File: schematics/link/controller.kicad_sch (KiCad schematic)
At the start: 55 parts, among them J6 Prog_Header, J7 SPI1, J8 SPI2, J9 Clock Jumper, SW5 BOOT0, SW6 RESET, U10 AT25SF128A-SHB-T, U7 ADS131M02QPWRQ1, U8 STM32G031K8Tx, U9 W5500, Y1 ECS-2520MVLC-081.92-BN-TR, Y2 KC2520Z25.0000C1SY00;

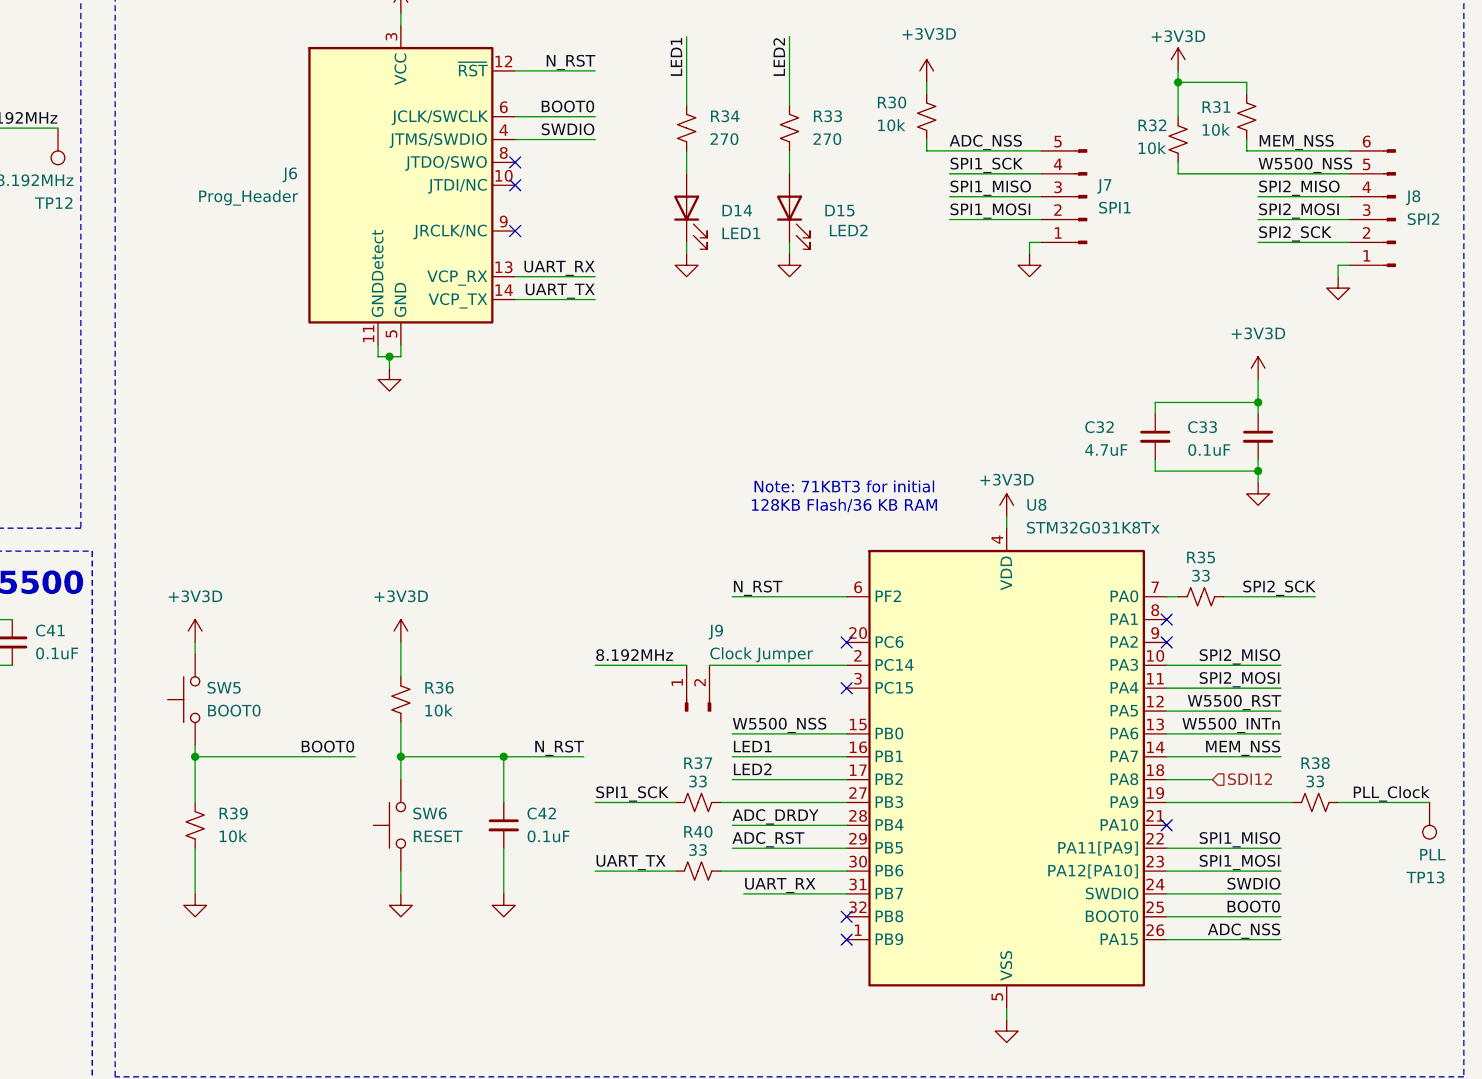
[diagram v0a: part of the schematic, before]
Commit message: update(pcb): combining modules
Want to try a different layout, but like where I am at right now
Planning to branch off of this one and see where it goes
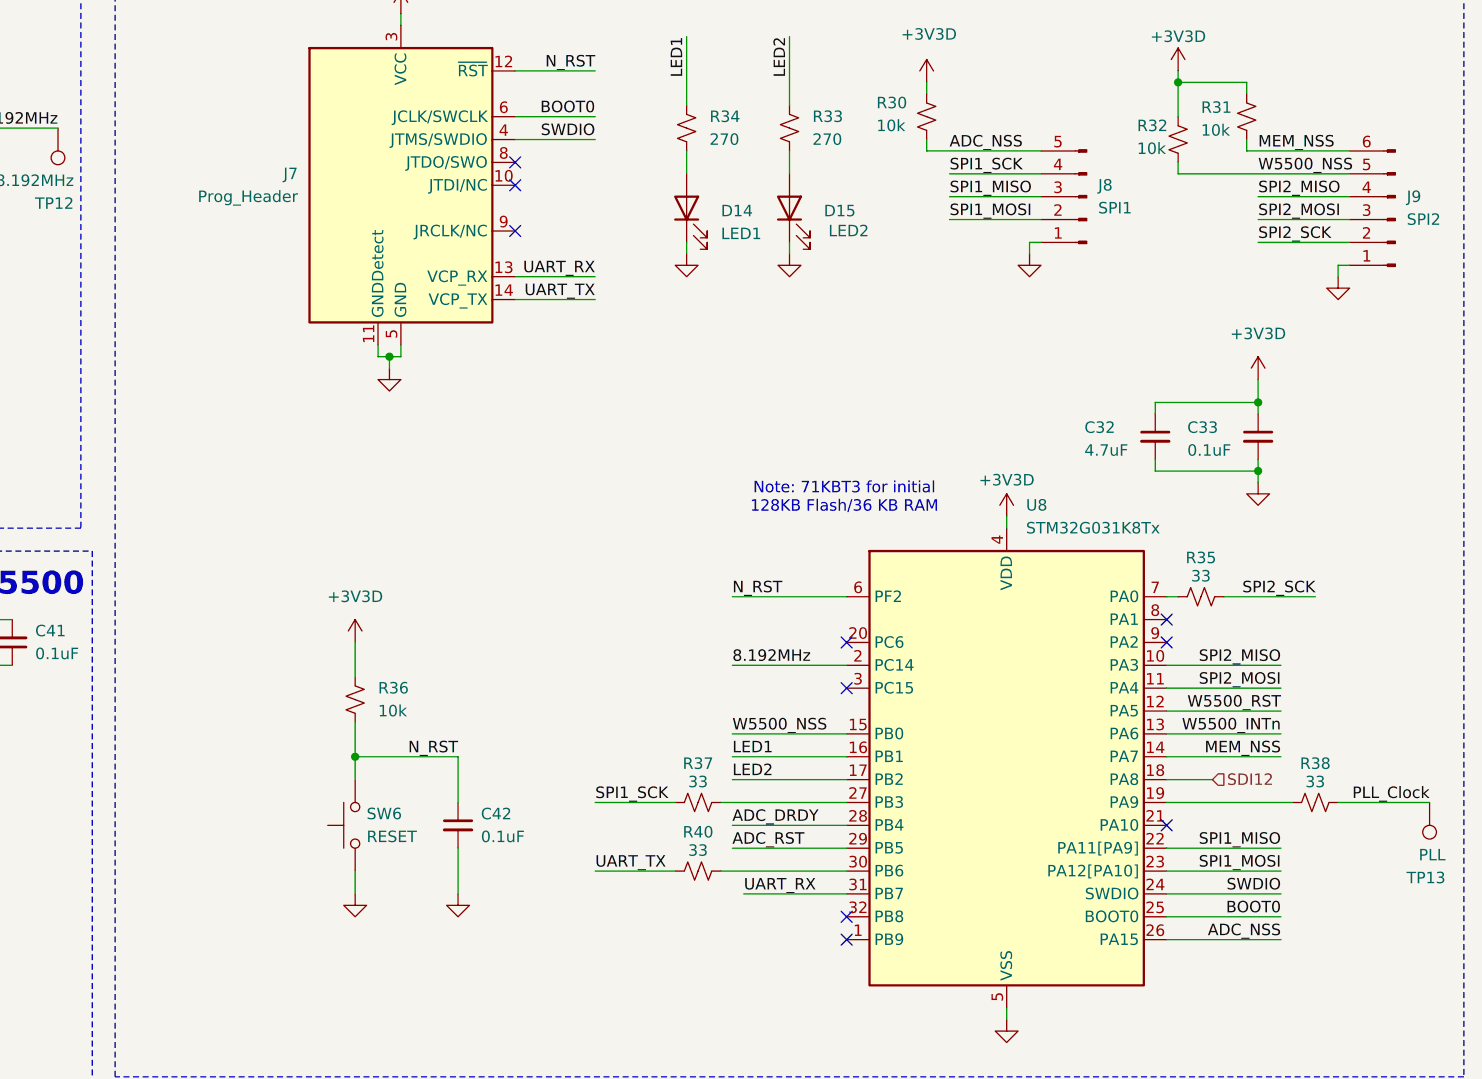
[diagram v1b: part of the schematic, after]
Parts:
- removed J9: Clock Jumper, Connector_PinHeader_2.54mm:PinHeader_1x02_P2.54mm_Vertical, symbol Connector:Conn_01x02_Pin
- removed R39: 10k, Resistor_SMD:R_0603_1608Metric, symbol Device:R_Small_US
- removed SW5: BOOT0, Link_Footprints:SW_TS04-66-55-BK-260-SMT, symbol Switch:SW_Push
- C32: footprint Capacitor_SMD:C_0402_1005Metric -> Capacitor_SMD:C_0603_1608Metric
- R30, R31, R32, R36, R41, R42: footprint Resistor_SMD:R_0603_1608Metric -> Resistor_SMD:R_0402_1005Metric
- renumbered J6 to J7, J7 to J8, J8 to J9
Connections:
- net 8.192MHz: now also U8.2 (PC14)
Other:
- moved on the sheet: C42, R36, SW6

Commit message: update(link): finalized placements
Still some work to be done:
1. Fix planes under RJ45 connector, probably should keep out if possible
2. Fix silkscreening
3. Fix isolated filled zones
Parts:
- removed C26, C28: 0.1uF, Capacitor_SMD:C_0402_1005Metric, symbol Device:C_Small
- removed D15: LED2, Diode_SMD:D_0603_1608Metric, symbol Device:LED
- removed J8: SPI1, Connector_PinHeader_2.54mm:PinHeader_1x05_P2.54mm_Vertical, symbol Connector:Conn_01x05_Pin
- removed J9: SPI2, Connector_PinHeader_2.54mm:PinHeader_1x06_P2.54mm_Vertical, symbol Connector:Conn_01x06_Pin
- removed R32: 10k, Resistor_SMD:R_0402_1005Metric, symbol Device:R_Small_US
- removed R34: 270, Resistor_SMD:R_0603_1608Metric, symbol Device:R_Small_US
- removed R40: 33, Resistor_SMD:R_0402_1005Metric, symbol Device:R_Small_US
- added R36: 10k, Resistor_SMD:R_0402_1005Metric, symbol Device:R_Small_US
- added R38: 33, Resistor_SMD:R_0402_1005Metric, symbol Device:R_Small_US
- R30: value 10k -> 270; footprint Resistor_SMD:R_0402_1005Metric -> Resistor_SMD:R_0603_1608Metric; LCSC Part # C95204 -> (none)
- R33: value 270 -> 10k; footprint Resistor_SMD:R_0603_1608Metric -> Resistor_SMD:R_0402_1005Metric; LCSC Part # C22369858 -> C95204; MPN RCA03270RFLF -> (none)
- R37: value 33 -> 10k; LCSC Part # C25105 -> C95204
- renumbered C29 to C27, C25 to C28, C30 to C29, C27 to C30, D14 to D10, J7 to J6, R36 to R32, R38 to R34, R41 to R39, R42 to R40, R43 to R41, SW6 to SW5
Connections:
- net +3V3A: now also U7.1 (AVDD)
- net +3V3A1: no longer U7.1 (AVDD)
- net +3V3D: now also R33.1, R37.1, R36.1; no longer R30.1
- net ADC_DRDY: now also U8.20 (PC6); no longer U8.28 (PB4)
- net ADC_NSS: now also R37.2; no longer R30.2
- net ADC_RST: now also U8.21 (PA10); no longer U8.29 (PB5)
- net MEM_NSS: now also U8.7 (PA0); no longer U8.14 (PA7)
- net SDI12: now also U8.9 (PA2); no longer U8.18 (PA8)
- net SPI1_SCK: now also R35.2; no longer R37.1
- net SPI2_MISO: now also U8.30 (PB6); no longer U8.10 (PA3)
- net SPI2_MOSI: now also U8.31 (PB7); no longer U8.11 (PA4)
- net SPI2_SCK: now also R38.2; no longer R35.2
- net UART_RX: now also U8.15 (PB0); no longer U8.31 (PB7)
- net UART_TX: now also U8.12 (PA5)
- net W5500_INTn: now also U8.28 (PB4); no longer U8.13 (PA6)
- net W5500_NSS: now also R33.2, U8.29 (PB5); no longer U8.15 (PB0)
- net W5500_RST: now also U8.1 (PB9), R36.2; no longer U8.12 (PA5)
- net at U8.27 (PB3): now also R35.1; no longer R37.2
- net at D10.2 (A): now also R30.2
- net at R34.1: now also U8.18 (PA8); no longer U8.19 (PA9)
- net at U8.32 (PB8): now also R38.1
- net LED1: no longer names the net of U8.16 (PB1)
- net LED2: no longer names the net of U8.17 (PB2)
- net LED2: no longer R33.1
- new net STATUS: R30.1, U8.10 (PA3)
- no-connect marks 22 -> 23
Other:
- moved on the sheet: C28, C30, C42, R32, R34, SW5, TP13

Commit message: fix: git history
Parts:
- added TP16, TP17: GND, Link_Footprints:TestPoint_Pad_D1.5mm, symbol Connector:TestPoint
- C42: MPN CGA0603X7R104K500JT -> (none)
- D10: MPN KT-0603B -> (none)
- R32: MPN RCA0310KJLF -> (none)
- SW5: MPN TS04-66-55-BK-260-SMT -> (none)
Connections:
- net GND: now also TP16.1, TP17.1
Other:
- note removed: "Note: 71KBT3 for initial 128KB Flash/36 KB RAM"

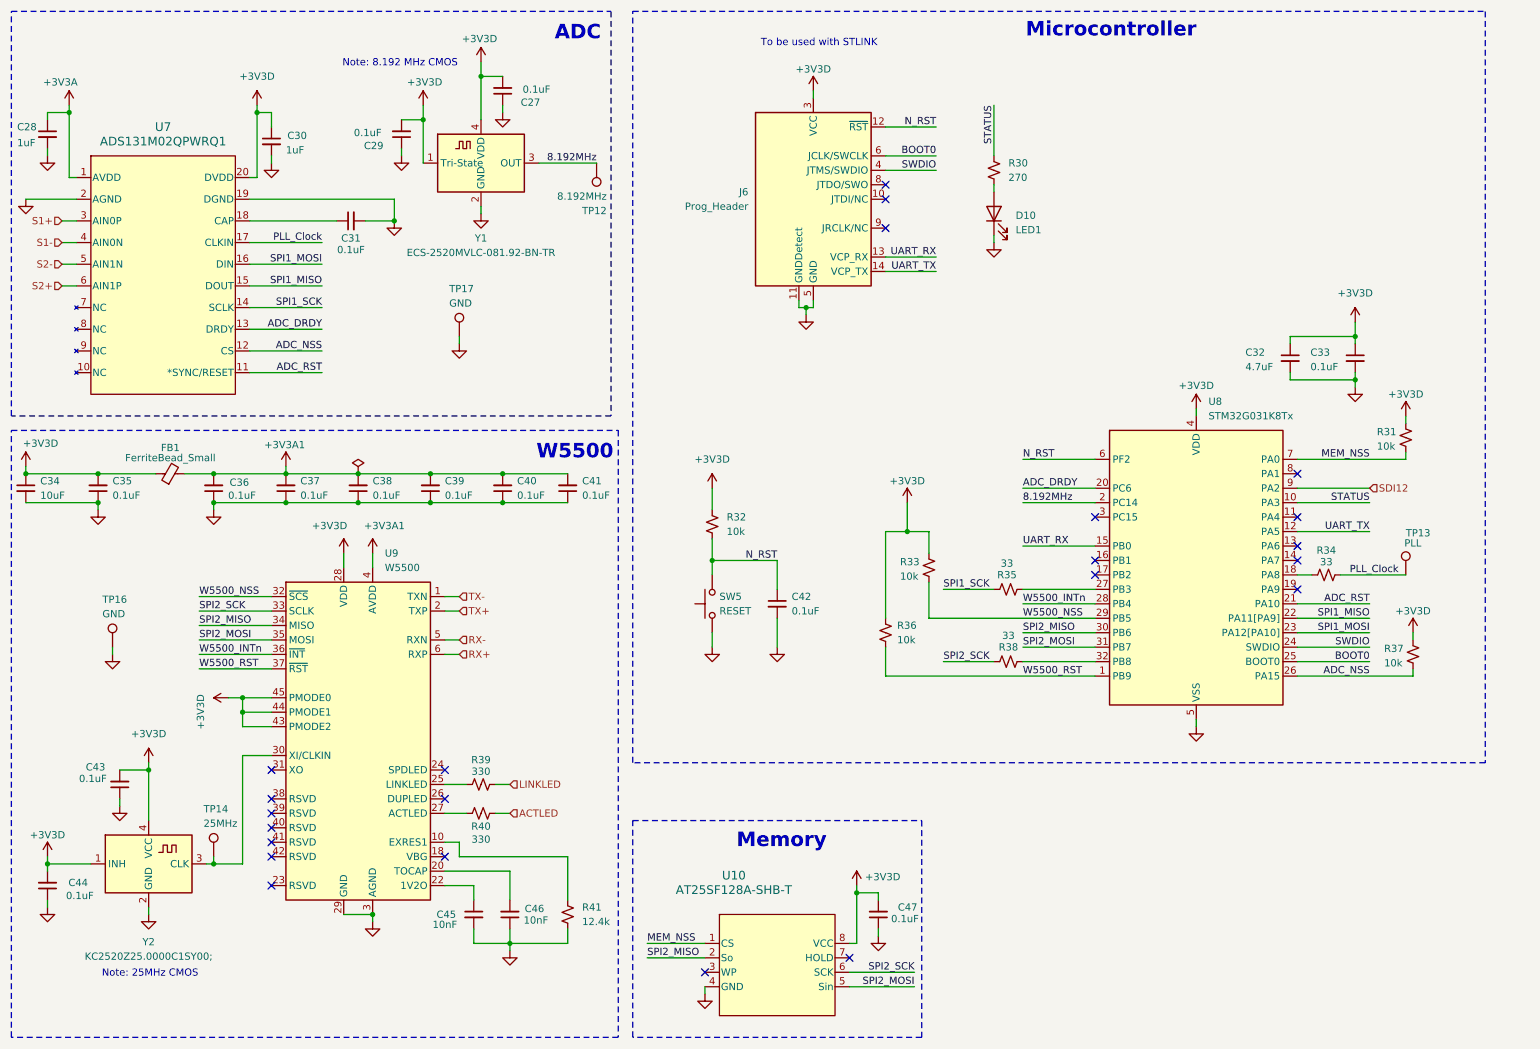
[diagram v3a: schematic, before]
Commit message: update(review):
1. Take gain resistor out of AFE filter
2. Breakout I2C
3. Move fuse to cover both 12V rails
4. Silkscreens
5. More testpoints + change to clip ons
6. Match ADC input max and filter output max
7. Add shunt for current resistors
8. Thermocouples
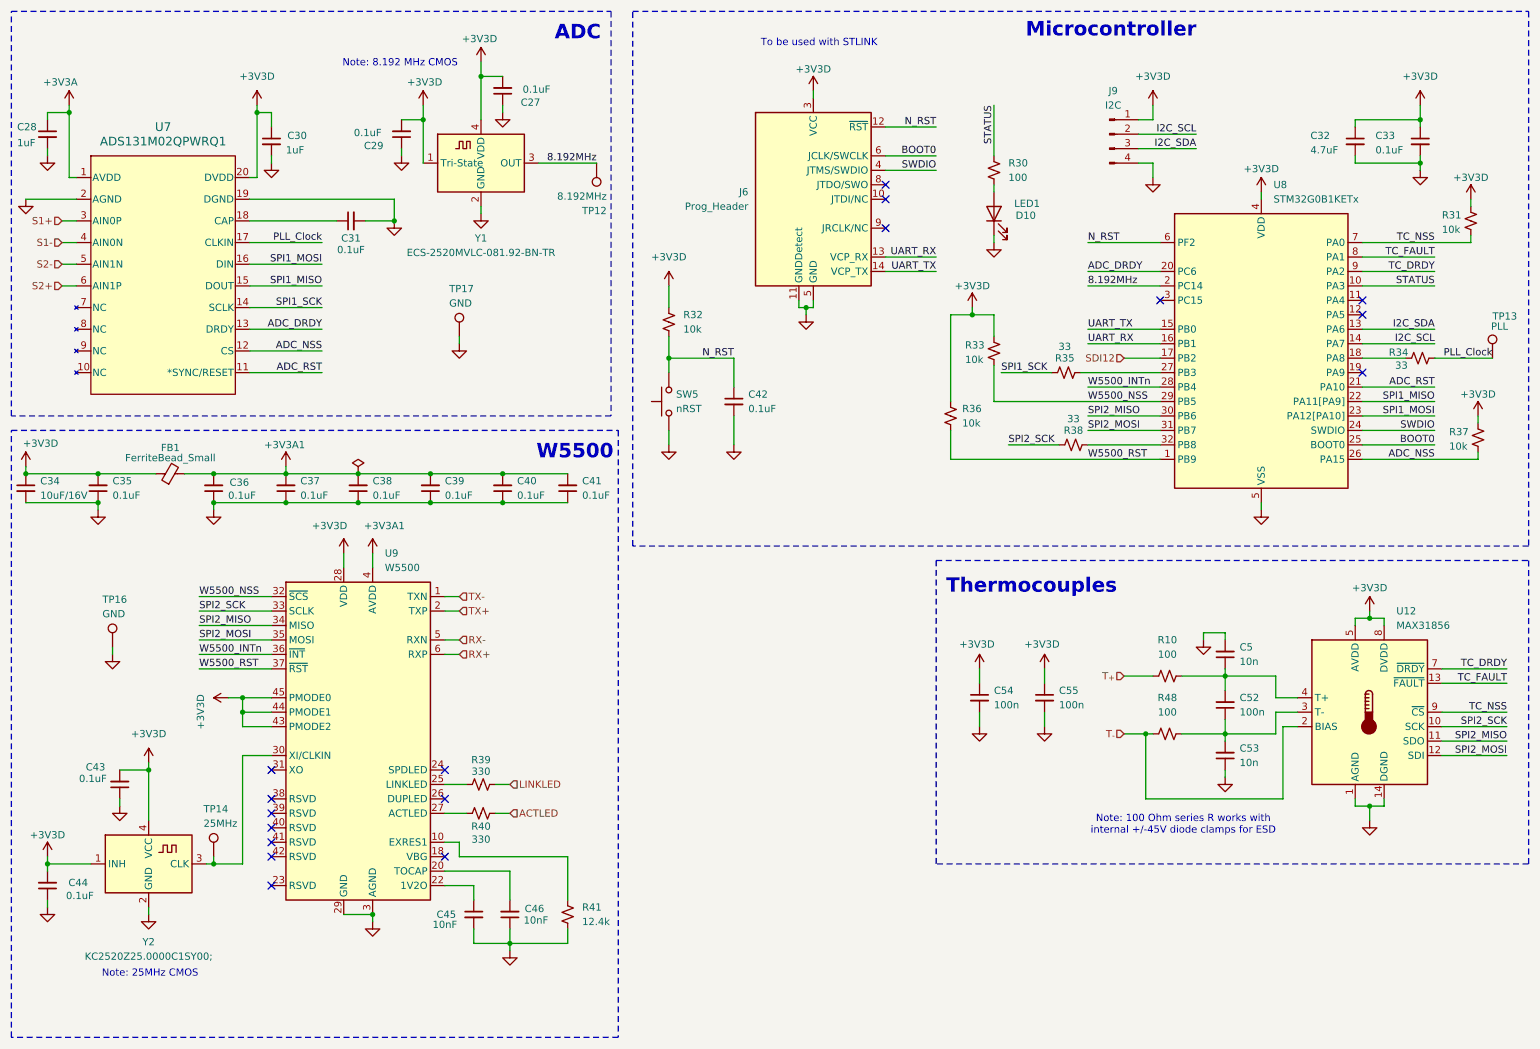
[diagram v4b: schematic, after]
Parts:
- removed C47: 0.1uF, Capacitor_SMD:C_0402_1005Metric, symbol Device:C_Small
- removed U10: AT25SF128A-SHB-T, Link_Footprints:AT25SF128A-SHB-T, symbol Link_Components:AT25SF128A-SHB-T
- removed U8: STM32G031K8Tx, Package_QFP:LQFP-32_7x7mm_P0.8mm, symbol Link_Components:STM32G031K6Tx
- added C5, C53: 10n, Capacitor_SMD:C_0402_1005Metric, symbol Device:C_Small
- added C52, C54, C55: 100n, Capacitor_SMD:C_0402_1005Metric, symbol Device:C_Small
- added J9: I2C, Connector_PinHeader_2.54mm:PinHeader_1x04_P2.54mm_Vertical, symbol Connector:Conn_01x04_Pin
- added R10, R48: 100, Resistor_SMD:R_0402_1005Metric, symbol Device:R_Small_US
- added U12: MAX31856, Package_SO:TSSOP-14_4.4x5mm_P0.65mm, symbol Link_Components:MAX31856
- added U8: STM32G0B1KETx, Package_QFP:LQFP-32_7x7mm_P0.8mm, symbol Link_Components:STM32G0B1KETx
- C27, C29, C31, C33, C35, C36, C37, C38, C39, C40, C41, C42, C43, C44: MPN (none) -> GRM155R71H104KE14D
- C28, C30: footprint Capacitor_SMD:C_0402_1005Metric -> Capacitor_SMD:C_0603_1608Metric; MPN (none) -> GCM188R71C105KA64D
- C32: MPN (none) -> GRM188Z71C475KE21D
- C34: value 10uF -> 10uF/16V; footprint Capacitor_SMD:C_0603_1608Metric -> Capacitor_SMD:C_0805_2012Metric; MPN (none) -> GCM21BR71A106KE22L
- C45, C46: MPN (none) -> GRM155R71H103KA88D
- D10: MPN (none) -> 150060BS75020
- FB1: MPN (none) -> MH1608-121Y
- J6: MPN (none) -> FTSH-107-01-L-DV-K
- R30: value 270 -> 100; MPN (none) -> RT0603BRD07100RL
- R31, R32, R33, R36, R37: MPN (none) -> RT0402BRD0710KL
- R34, R35, R38: MPN (none) -> RC0402FR-0733RL
- R39, R40: MPN (none) -> RC0402FR-07330RL
- R41: MPN (none) -> AC0402FR-0712K4L
- SW5: value RESET -> nRST; MPN (none) -> TS04-66-55-BK-260-SMT
- TP12, TP13, TP14: MPN (none) -> N/A
- TP16, TP17: footprint Link_Footprints:TestPoint_Pad_D1.5mm -> Link_Footprints:Keystone1573-2; MPN (none) -> 1573-2; now in the parts list
- U7: MPN (none) -> ADS131M02IPWR
- U9: MPN (none) -> W5500
- Y1: MPN (none) -> ECS-2520MVLC-081.92-BN-TR
- Y2: MPN (none) -> KC2520Z25.0000C15XXK
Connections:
- net +3V3D: now also C54.1, C55.1, J9.1 (Pin_1), U12.5 (AVDD), U12.8 (DVDD), U8.4 (VDD)
- net 8.192MHz: now also U8.2 (PC14)
- net ADC_DRDY: now also U8.20 (PC6)
- net ADC_NSS: now also U8.26 (PA15)
- net ADC_RST: now also U8.21 (PA10)
- net BOOT0: now also U8.25 (BOOT0)
- net GND: now also C5.2, C53.1, C54.2, C55.2, J9.4 (Pin_4), U12.1 (AGND), U12.14 (DGND), U8.5 (VSS)
- net N_RST: now also U8.6 (PF2)
- net SDI12: now also U8.17 (PB2)
- net SPI1_MISO: now also U8.22 (PA11[PA9])
- net SPI1_MOSI: now also U8.23 (PA12[PA10])
- net SPI2_MISO: now also U12.11 (SDO), U8.30 (PB6)
- net SPI2_MOSI: now also U12.12 (SDI), U8.31 (PB7)
- net SPI2_SCK: now also U12.10 (SCK)
- net STATUS: now also U8.10 (PA3)
- net SWDIO: now also U8.24 (SWDIO)
- net UART_RX: now also U8.16 (PB1)
- net UART_TX: now also U8.15 (PB0)
- net W5500_INTn: now also U8.28 (PB4)
- net W5500_NSS: now also U8.29 (PB5)
- net W5500_RST: now also U8.1 (PB9)
- net at R38.1: now also U8.32 (PB8)
- net at R34.1: now also U8.18 (PA8)
- net at R35.1: now also U8.27 (PB3)
- net MEM_NSS renamed TC_NSS
- net TC_NSS: now also U12.9 (~{CS}), U8.7 (PA0)
- new net: C52.1, C53.2, R48.2, U12.3 (T-)
- new net: C5.1, C52.2, R10.2, U12.4 (T+)
- new net I2C_SCL: J9.2 (Pin_2), U8.14 (PA7)
- new net I2C_SDA: J9.3 (Pin_3), U8.13 (PA6)
- new net TC_DRDY: U12.7 (~{DRDY}), U8.9 (PA2)
- new net TC_FAULT: U12.13 (~{FAULT}), U8.8 (PA1)
- new net T_{+}: R10.1
- new net T_{-}: R48.1, U12.2 (BIAS)
- no-connect marks 23 -> 17
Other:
- note added: "Note: 100 Ohm series R works with internal +/-45V diode clamps for ESD"
- note added: "Thermocouples"
- note removed: "Memory"
- moved on the sheet: C32, C33, C42, R31, R32, R33, R34, R35, R36, R37, R38, SW5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

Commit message: GPT review
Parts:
- added R49, R50: 3.3k, Resistor_SMD:R_0402_1005Metric, symbol Device:R_Small_US
- added R51: 10k, Resistor_SMD:R_0402_1005Metric, symbol Device:R_Small_US
- C46: value 10nF -> 4.7uF; MPN GRM155R71H103KA88D -> GRM155R60G475ME47J
- C5, C53: value 10n -> 10nF; LCSC C327204 -> (none); MPN CC0603KRX7R8BB103 -> GRM155R71H103KA88D
- C52, C54, C55: value 100n -> 0.1uF; LCSC C6119867 -> (none); MPN CGA0603X7R104K500JT -> GRM155R71H104KE14D
- R10, R48: LCSC C22356621 -> (none)
- U12: LCSC C2653162 -> (none)
- U7: value ADS131M02QPWRQ1 -> ADS131M02IPWR; LCSC Part # C5549016 -> (none)
- U8: LCSC Part # C529348 -> (none); MPN STM32G0B1KET6N -> STM32G0B1KET6
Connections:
- net +3V3D: now also R49.1, R50.1
- net BOOT0: now also R51.1
- net GND: now also R51.2
- net I2C_SCL: now also R49.2
- net I2C_SDA: now also R50.2
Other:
- moved on the sheet: J6, J9
